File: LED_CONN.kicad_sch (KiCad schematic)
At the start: 7 parts, among them U3 SM02B-SRSS-TB-LF-SN, U4 SM02B-SRSS-TB-LF-SN

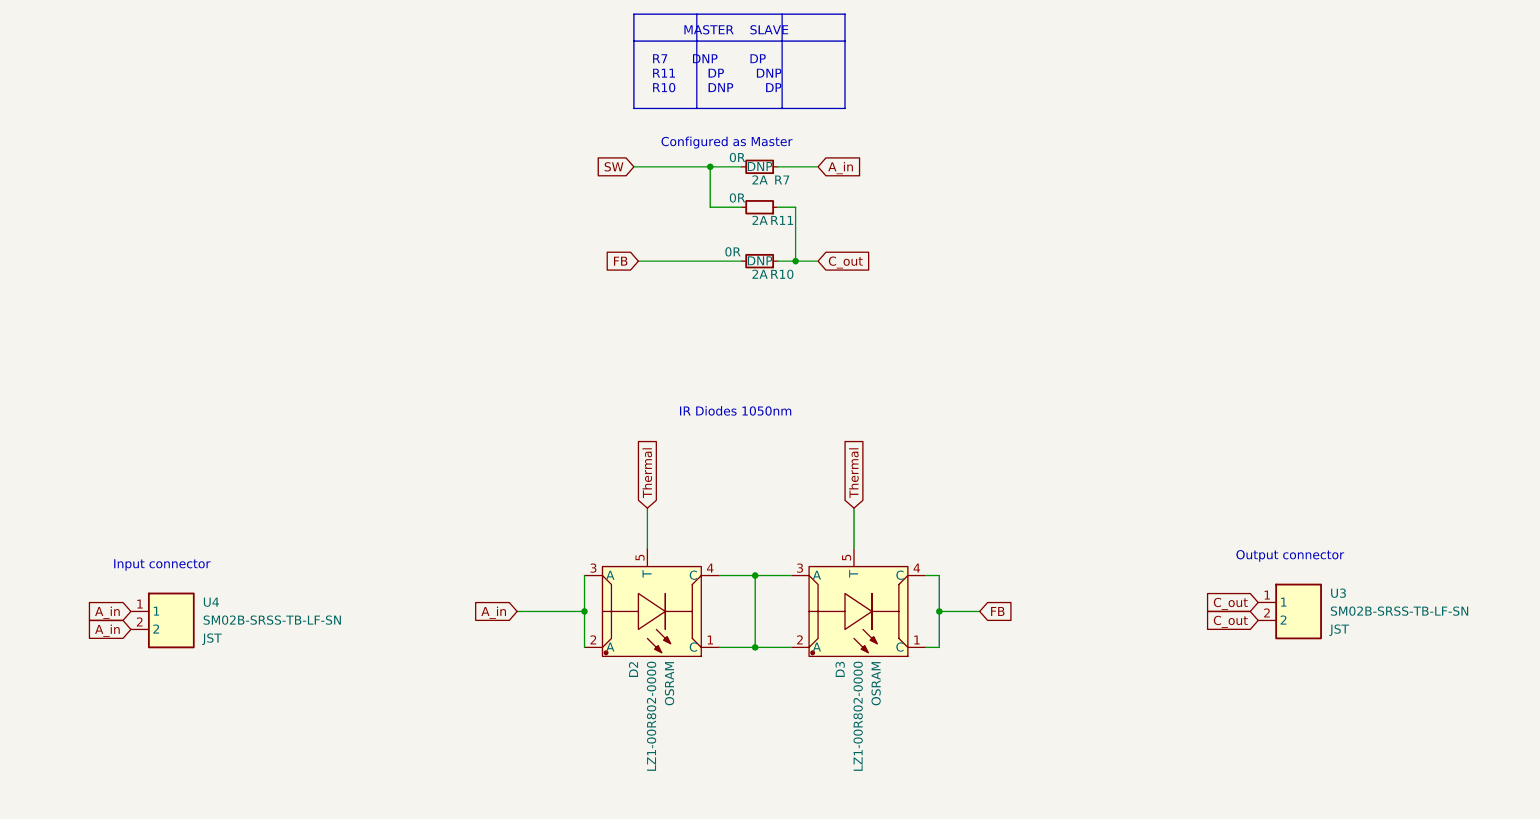
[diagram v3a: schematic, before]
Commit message: B2B connectors symbol adjusted
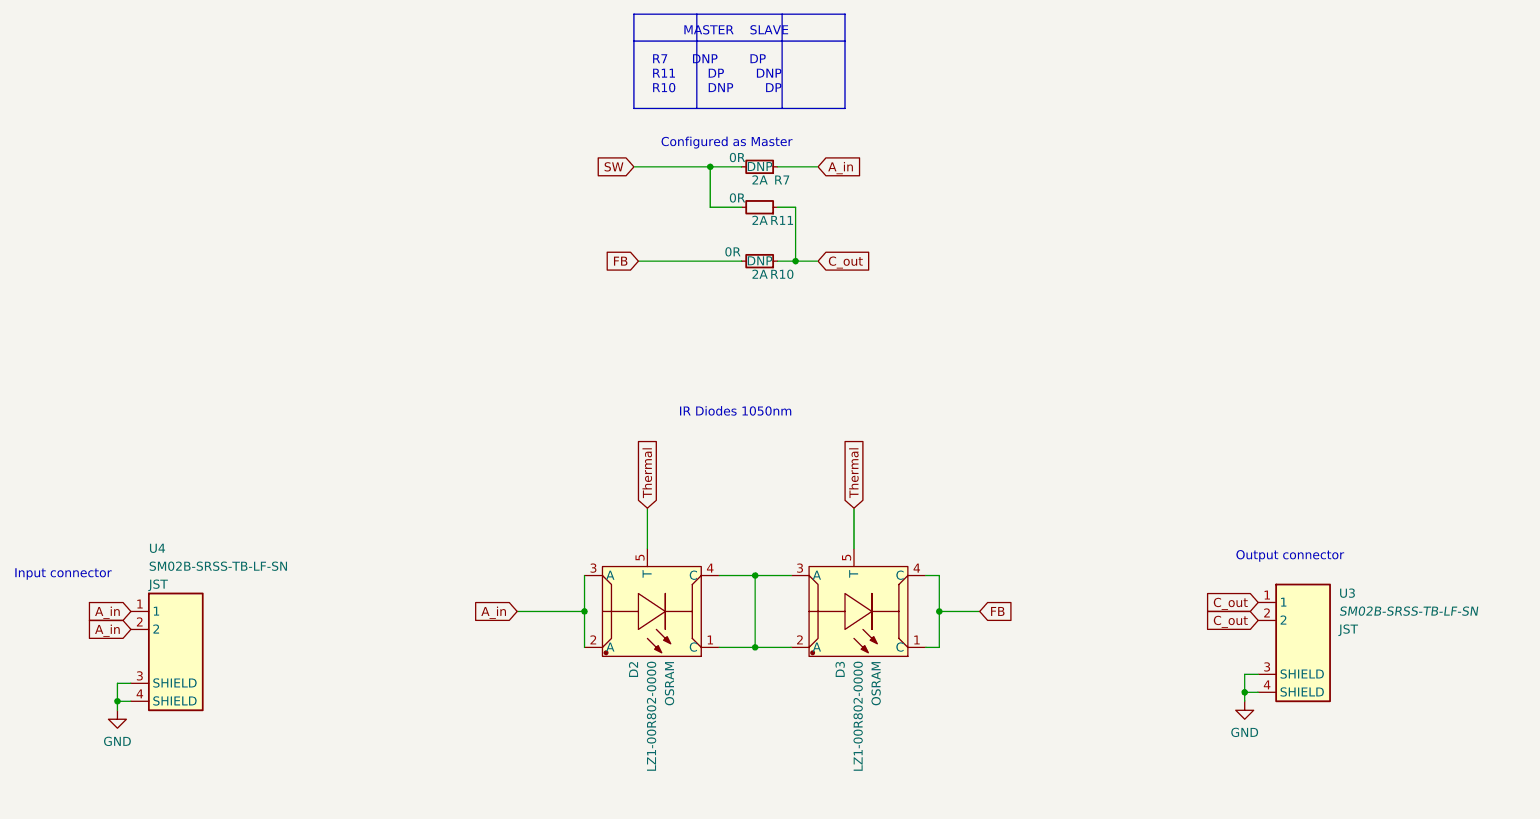
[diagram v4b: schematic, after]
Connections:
- new net GND: U3.3 (SHIELD), U3.4 (SHIELD), U4.3 (SHIELD), U4.4 (SHIELD)
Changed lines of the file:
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@@
 (kicad_sch (version 20211123) (generator eeschema)
   (paper "A4")
+  (junction (at 60.325 114.935) (diameter 0) (color 0 0 0 0)
+  )
   (junction (at 144.145 39.37) (diameter 0) (color 0 0 0 0)
   )
   (junction (at 156.21 52.705) (diameter 0) (color 0 0 0 0)
   )
+  (junction (at 219.71 113.665) (diameter 0) (color 0 0 0 0)
+  )
   (junction (at 176.53 102.235) (diameter 0) (color 0 0 0 0)
   )
@@
     (stroke (width 0) (type default) (color 0 0 0 0))
   )
+  (wire (pts (xy 219.71 113.665) (xy 221.615 113.665))
+    (stroke (width 0) (type default) (color 0 0 0 0))
+  )
   (wire (pts (xy 145.415 97.155) (xy 150.495 97.155))
     (stroke (width 0) (type default) (color 0 0 0 0))
@@
     (stroke (width 0) (type default) (color 0 0 0 0))
   )
+  (wire (pts (xy 219.71 113.665) (xy 219.71 114.935))
+    (stroke (width 0) (type default) (color 0 0 0 0))
+  )
   (polyline (pts (xy 163.195 17.78) (xy 163.195 31.115))
     (stroke (width 0) (type default) (color 0 0 0 0))
@@
     (stroke (width 0) (type default) (color 0 0 0 0))
   )
+  (wire (pts (xy 219.71 111.125) (xy 219.71 113.665))
+    (stroke (width 0) (type default) (color 0 0 0 0))
+  )
   (wire (pts (xy 150.495 97.155) (xy 150.495 107.315))
     (stroke (width 0) (type default) (color 0 0 0 0))
@@
     (stroke (width 0) (type default) (color 0 0 0 0))
   )
+  (wire (pts (xy 60.325 114.935) (xy 62.23 114.935))
+    (stroke (width 0) (type default) (color 0 0 0 0))
+  )
   (wire (pts (xy 176.53 107.315) (xy 176.53 102.235))
     (stroke (width 0) (type default) (color 0 0 0 0))
@@
     (stroke (width 0) (type default) (color 0 0 0 0))
   )
+  (wire (pts (xy 60.325 112.395) (xy 60.325 114.935))
+    (stroke (width 0) (type default) (color 0 0 0 0))
+  )
   (wire (pts (xy 144.145 39.37) (xy 144.145 45.085))
     (stroke (width 0) (type default) (color 0 0 0 0))
@@
     (stroke (width 0) (type default) (color 0 0 0 0))
   )
+  (wire (pts (xy 62.23 112.395) (xy 60.325 112.395))
+    (stroke (width 0) (type default) (color 0 0 0 0))
+  )
   (polyline (pts (xy 154.305 17.78) (xy 154.305 31.115))
     (stroke (width 0) (type default) (color 0 0 0 0))
@@
     (stroke (width 0) (type default) (color 0 0 0 0))
   )
+  (wire (pts (xy 221.615 111.125) (xy 219.71 111.125))
+    (stroke (width 0) (type default) (color 0 0 0 0))
+  )
   (wire (pts (xy 156.21 45.085) (xy 156.21 52.705))
     (stroke (width 0) (type default) (color 0 0 0 0))
@@
   )
   (wire (pts (xy 126.365 107.315) (xy 126.365 102.235))
+    (stroke (width 0) (type default) (color 0 0 0 0))
+  )
+  (wire (pts (xy 60.325 114.935) (xy 60.325 116.205))
     (stroke (width 0) (type default) (color 0 0 0 0))
   )
@@
     (effects (font (size 1.27 1.27)) (justify left bottom))
   )
-  (text "Input connector" (at 59.69 96.52 0)
+  (text "Input connector" (at 45.72 97.79 0)
     (effects (font (size 1.27 1.27)) (justify left bottom))
   )
@@
     (pin "5")
   )
-  (symbol (lib_id "antmicroRectangularConnectorsHeadersMalePins:SM02B-SRSS-TB-LF-SN") (at 221.615 100.965 0) (unit 1)
-    (in_bom yes) (on_board yes) (fields_autoplaced)
-    (property "Reference" "U3" (id 0) (at 231.775 99.6949 0)
-      (effects (font (size 1.27 1.27)) (justify left))
-    )
-    (property "Value" "SM02B-SRSS-TB-LF-SN" (id 1) (at 231.775 102.2349 0)
-      (effects (font (size 1.27 1.27)) (justify left))
-    )
-    (property "Footprint" "antmicro-footprints:JST_SM02B-SRSS-TB(LF)(SN)" (id 2) (at 259.715 111.125 0)
-      (effects (font (size 1.27 1.27)) hide)
-    )
-    (property "Datasheet" "https://www.farnell.com/datasheets/2082363.pdf" (id 3) (at 259.715 103.505 0)
-      (effects (font (size 1.27 1.27)) hide)
-    )
-    (property "MPN" "SM02B-SRSS-TB (LF)(SN)" (id 4) (at 248.285 106.045 0)
-      (effects (font (size 1.27 1.27)) hide)
-    )
-    (property "Manufacturer" "JST" (id 5) (at 231.775 104.7749 0)
-      (effects (font (size 1.27 1.27)) (justify left))
-    )
-    (property "Copyright" "Copyright (c) 2023 Antmicro" (id 6) (at 249.555 108.585 0)
-      (effects (font (size 1.27 1.27)) hide)
-    )
-    (property "License" "Apache-2.0 License" (id 7) (at 245.745 100.965 0)
-      (effects (font (size 1.27 1.27)) hide)
-    )
-    (pin "1")
-    (pin "2")
+  (symbol (lib_id "power:GND") (at 60.325 116.205 0) (unit 1)
+    (in_bom yes) (on_board yes) (fields_autoplaced)
+    (property "Reference" "#PWR?" (id 0) (at 60.325 122.555 0)
+      (effects (font (size 1.27 1.27)) hide)
+    )
+    (property "Value" "GND" (id 1) (at 60.325 120.65 0))
+    (property "Footprint" "" (id 2) (at 60.325 116.205 0)
+      (effects (font (size 1.27 1.27)) hide)
+    )
+    (property "Datasheet" "" (id 3) (at 60.325 116.205 0)
+      (effects (font (size 1.27 1.27)) hide)
+    )
+    (pin "1")
+  )
+  (symbol (lib_id "antmicroRectangularConnectorsHeadersMalePins:SM02B-SRSS-TB-LF-SN") (at 222.885 100.965 0) (unit 1)
+    (in_bom yes) (on_board yes) (fields_autoplaced)
+    (property "Reference" "U3" (id 0) (at 233.045 99.6949 0)
+      (effects (font (size 1.27 1.27)) (justify left))
+    )
+    (property "Value" "SM02B-SRSS-TB-LF-SN" (id 1) (at 233.045 102.2349 0)
+      (effects (font (size 1.27 1.27) italic) (justify left))
+    )
+    (property "Footprint" "antmicro-footprints:JST_SM02B-SRSS-TB(LF)(SN)" (id 2) (at 260.985 111.125 0)
+      (effects (font (size 1.27 1.27)) hide)
+    )
+    (property "Datasheet" "https://www.farnell.com/datasheets/2082363.pdf" (id 3) (at 260.985 103.505 0)
+      (effects (font (size 1.27 1.27)) hide)
+    )
+    (property "MPN" "SM02B-SRSS-TB (LF)(SN)" (id 4) (at 249.555 106.045 0)
+      (effects (font (size 1.27 1.27)) hide)
+    )
+    (property "Manufacturer" "JST" (id 5) (at 233.045 104.7749 0)
+      (effects (font (size 1.27 1.27)) (justify left))
+    )
+    (property "Copyright" "Copyright (c) 2023 Antmicro" (id 6) (at 250.825 108.585 0)
+      (effects (font (size 1.27 1.27)) hide)
+    )
+    (property "License" "Apache-2.0 License" (id 7) (at 247.015 100.965 0)
+      (effects (font (size 1.27 1.27)) hide)
+    )
+    (pin "1")
+    (pin "2")
+    (pin "3")
+    (pin "4")
+  )
+  (symbol (lib_id "power:GND") (at 219.71 114.935 0) (unit 1)
+    (in_bom yes) (on_board yes) (fields_autoplaced)
+    (property "Reference" "#PWR?" (id 0) (at 219.71 121.285 0)
+      (effects (font (size 1.27 1.27)) hide)
+    )
+    (property "Value" "GND" (id 1) (at 219.71 119.38 0))
+    (property "Footprint" "" (id 2) (at 219.71 114.935 0)
+      (effects (font (size 1.27 1.27)) hide)
+    )
+    (property "Datasheet" "" (id 3) (at 219.71 114.935 0)
+      (effects (font (size 1.27 1.27)) hide)
+    )
+    (pin "1")
   )
   (symbol (lib_id "antmicroLEDIndicationDiscrete:LZ1-00R802-0000") (at 145.415 107.315 180) (unit 1)
@@
     (pin "2")
   )
-  (symbol (lib_id "antmicroRectangularConnectorsHeadersMalePins:SM02B-SRSS-TB-LF-SN") (at 62.23 102.235 0) (unit 1)
-    (in_bom yes) (on_board yes) (fields_autoplaced)
-    (property "Reference" "U4" (id 0) (at 72.39 100.9649 0)
-      (effects (font (size 1.27 1.27)) (justify left))
-    )
-    (property "Value" "SM02B-SRSS-TB-LF-SN" (id 1) (at 72.39 103.5049 0)
+  (symbol (lib_name "SM02B-SRSS-TB-LF-SN_1") (lib_id "antmicroRectangularConnectorsHeadersMalePins:SM02B-SRSS-TB-LF-SN") (at 62.23 102.235 0) (unit 1)
+    (in_bom yes) (on_board yes) (fields_autoplaced)
+    (property "Reference" "U4" (id 0) (at 64.77 93.3449 0)
+      (effects (font (size 1.27 1.27)) (justify left))
+    )
+    (property "Value" "SM02B-SRSS-TB-LF-SN" (id 1) (at 64.77 95.8849 0)
       (effects (font (size 1.27 1.27)) (justify left))
     )
@@
       (effects (font (size 1.27 1.27)) hide)
     )
-    (property "Manufacturer" "JST" (id 5) (at 72.39 106.0449 0)
+    (property "Manufacturer" "JST" (id 5) (at 64.77 98.4249 0)
       (effects (font (size 1.27 1.27)) (justify left))
     )
@@
     (pin "1")
     (pin "2")
+    (pin "3")
+    (pin "4")
   )
 )

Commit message: Finalized board layout
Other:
- note added: "DEBUG"
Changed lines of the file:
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@@
+    (effects (font (size 1.27 1.27)) (justify left bottom))
+  )
+  (text "DEBUG" (at 126.365 24.765 0)
     (effects (font (size 1.27 1.27)) (justify left bottom))
   )
@@
   (symbol (lib_id "power:GND") (at 60.325 116.205 0) (unit 1)
     (in_bom yes) (on_board yes) (fields_autoplaced)
-    (property "Reference" "#PWR?" (id 0) (at 60.325 122.555 0)
+    (property "Reference" "#PWR0103" (id 0) (at 60.325 122.555 0)
       (effects (font (size 1.27 1.27)) hide)
     )
@@
   (symbol (lib_id "power:GND") (at 219.71 114.935 0) (unit 1)
     (in_bom yes) (on_board yes) (fields_autoplaced)
-    (property "Reference" "#PWR?" (id 0) (at 219.71 121.285 0)
+    (property "Reference" "#PWR0102" (id 0) (at 219.71 121.285 0)
       (effects (font (size 1.27 1.27)) hide)
     )
